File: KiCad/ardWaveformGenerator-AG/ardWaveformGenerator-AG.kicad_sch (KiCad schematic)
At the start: 39 parts, among them SW1 SW_Rotary1x4, U1 Power in, U2 LM386, U3 Output

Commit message: ardWaveformGenerator-AG-pio with pcb-0.2
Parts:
- removed R12, R14, R18, R21: 20k, My_Parts:R_Axial_parallell_DIN0207_L6.3mm_D2.5mm_P10.16mm_Horizontal_large, symbol Device:R
- added R10, R17, R19, R23, R25, R26, R28, R29, R3, R30, R31, R7, R9: 10k, My_Misc:R_Axial_DIN0207_L6.3mm_D2.5mm_P10.16mm_Horizontal_large, symbol Device:R
- added R32: 2.2k, My_Misc:R_Axial_DIN0207_L6.3mm_D2.5mm_P10.16mm_Horizontal_large, symbol Device:R
- R1, R16, R2, R20, R4, R6: value 20k -> 10k; footprint My_Parts:R_Axial_parallell_DIN0207_L6.3mm_D2.5mm_P10.16mm_Horizontal_large -> My_Misc:R_Axial_DIN0207_L6.3mm_D2.5mm_P10.16mm_Horizontal_large
- R22: value 2.2k -> 10k
- renumbered R8 to R11, R9 to R12, R10 to R13, R11 to R14, R7 to R15, R13 to R18, R15 to R21, R17 to R24, R19 to R27, R23 to R33, R24 to R34, R25 to R35, R26 to R36, R3 to R5, R5 to R8
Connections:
- net D0: now also R4.1; no longer R2.1
- net D1: now also R7.1; no longer R4.1
- net D2: now also R10.1; no longer R6.1
- net D3: now also R17.1
- net D4: now also R20.1
- net D5: now also R23.1; no longer R16.1
- net D6: now also R26.1
- net D7: now also R29.1; no longer R20.1
- net GND: now also R2.1, R32.2; no longer R1.1, R22.2
- net at R24.2, R27.1: now also R25.2
- net at C1.1, R27.2: now also R28.2; no longer R20.2
- net at R15.2, R18.1: now also R16.2
- net at R22.1: now also R23.2; no longer U2.3 (+)
- net at R1.2, R5.1: now also R3.2; no longer R2.2
- net at R5.2, R8.1: now also R6.2; no longer R4.2
- net at R18.2, R21.1: now also R19.2
- net at C1.2: now also R30.2
- net at R15.1, R8.2: now also R9.2; no longer R6.2
- net at R21.2, R24.1: now also R22.2; no longer R16.2
- new net: R10.2, R9.1
- new net: R30.1, R31.2
- new net: R6.1, R7.2
- new net: R31.1, R32.1, U2.3 (+)
- new net: R28.1, R29.2
- new net: R16.1, R17.2
- new net: R25.1, R26.2
- new net: R19.1, R20.2
- new net: R1.1, R2.2
- new net: R3.1, R4.2
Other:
- moved on the sheet: C1, R15, R18, R21, R24, R27, R5, R8

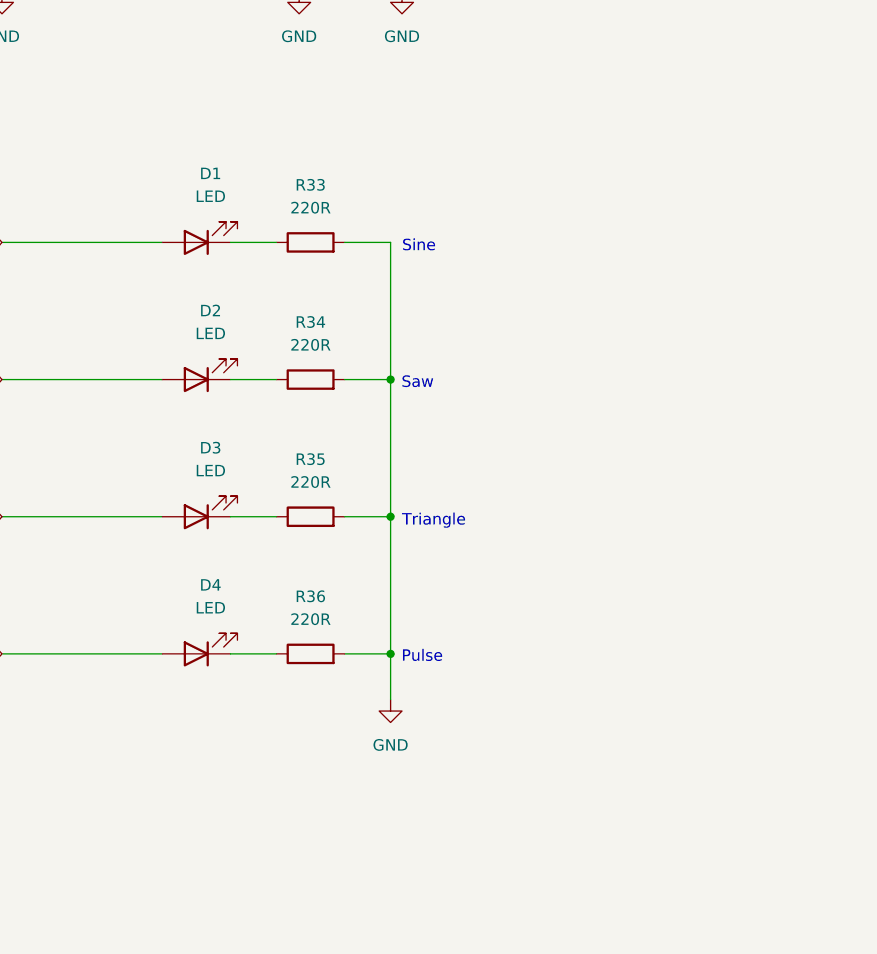
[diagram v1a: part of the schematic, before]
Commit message: LED-header on pcb, version 0.3
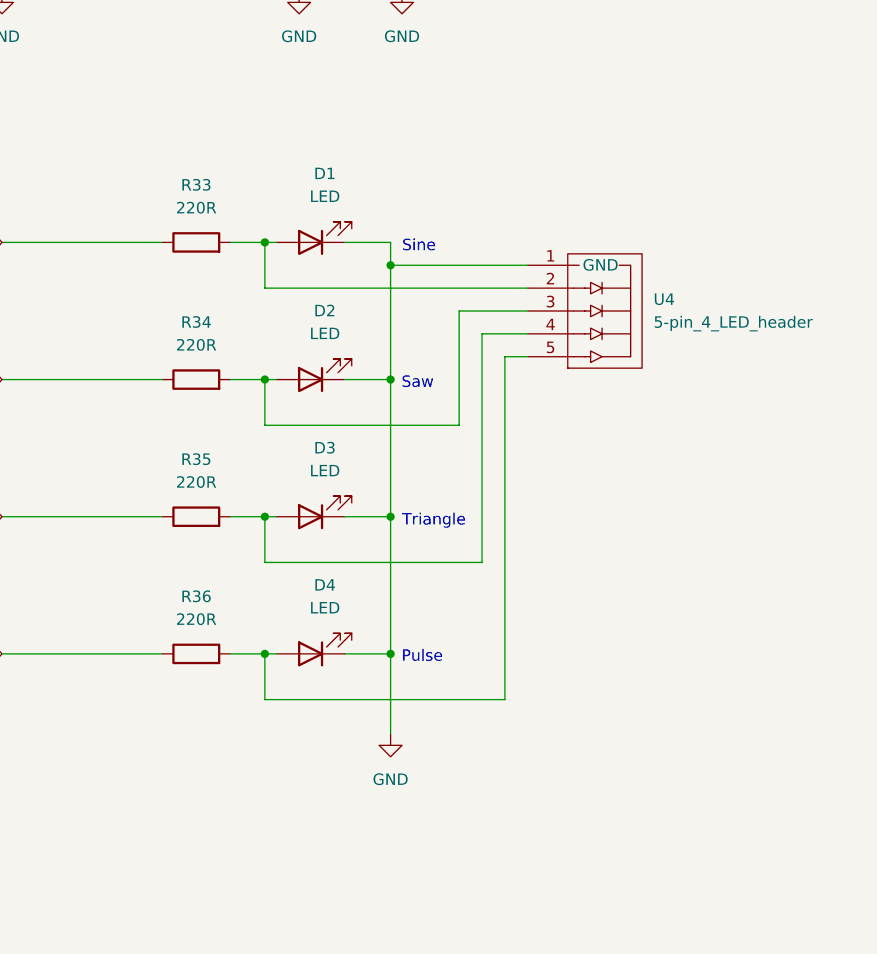
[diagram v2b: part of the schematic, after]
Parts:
- added U4: 5-pin_4_LED_header, My_Headers:5-pin JST 4-LED, symbol My_Headers:5-pin_4_LED_header
- D1, D2, D3, D4: footprint My_Misc:LED_D5.0mm_large -> (none)
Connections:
- net D10: now also R35.1; no longer D3.2 (A)
- net D11: now also R36.1; no longer D4.2 (A)
- net D8: now also R33.1; no longer D1.2 (A)
- net D9: now also R34.1; no longer D2.2 (A)
- net GND: now also D1.1 (K), D2.1 (K), D3.1 (K), D4.1 (K), U4.1 (GND); no longer R33.2, R34.2, R35.2, R36.2
- new net: D1.2 (A), R33.2, U4.2
- new net: D4.2 (A), R36.2, U4.5
- new net: D2.2 (A), R34.2, U4.3
- new net: D3.2 (A), R35.2, U4.4

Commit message: new buttons
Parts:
- removed SW1: SW_Rotary1x4, My_Headers:5-pin JST SW_Rotary1x4, symbol My_Parts:SW_Rotary1x4
- added SW1, SW2, SW3, SW4: SW_Push, symbol Switch:SW_Push
- added U2: 5-pin_4_buttons_+_common, My_Headers:5-pin JST 4 buttons + common, symbol My_Headers:5-pin_4_buttons_+_common
- renumbered U2 to U3, U3 to U4, U4 to U5
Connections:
- net A0: now also SW1.2, U2.2 (But1)
- net A1: now also SW2.2, U2.3 (But2)
- net A2: now also SW3.2, U2.4 (But3)
- net A3: now also SW4.2, U2.5 (But4)
- net GND: now also SW1.1, SW2.1, SW3.1, SW4.1, U2.1 (Com)
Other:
- moved on the sheet: U1

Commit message: VeroRoute and AG v0.4
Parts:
- R1, R10, R11, R12, R13, R14, R15, R16, R17, R18, R19, R2, R20, R21, R22, R23, R24, R25, R26, R27, R28, R29, R3, R30, R31, R32, R33, R34, R35, R36, R4, R5, R6, R7, R8, R9: footprint My_Misc:R_Axial_DIN0207_L6.3mm_D2.5mm_P10.16mm_Horizontal_large -> My_Misc:R_Axial_DIN0207_L6.3mm_D2.5mm_P2.54mm_Vertical_large
